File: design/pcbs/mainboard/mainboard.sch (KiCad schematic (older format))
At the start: 15 parts, among them J1 Conn_Coaxial, J15 Conn_01x01, J16 Conn_01x01, J17 Conn_01x01, J18 Conn_01x01, J2 Conn_Coaxial, J4 AudioJackSw

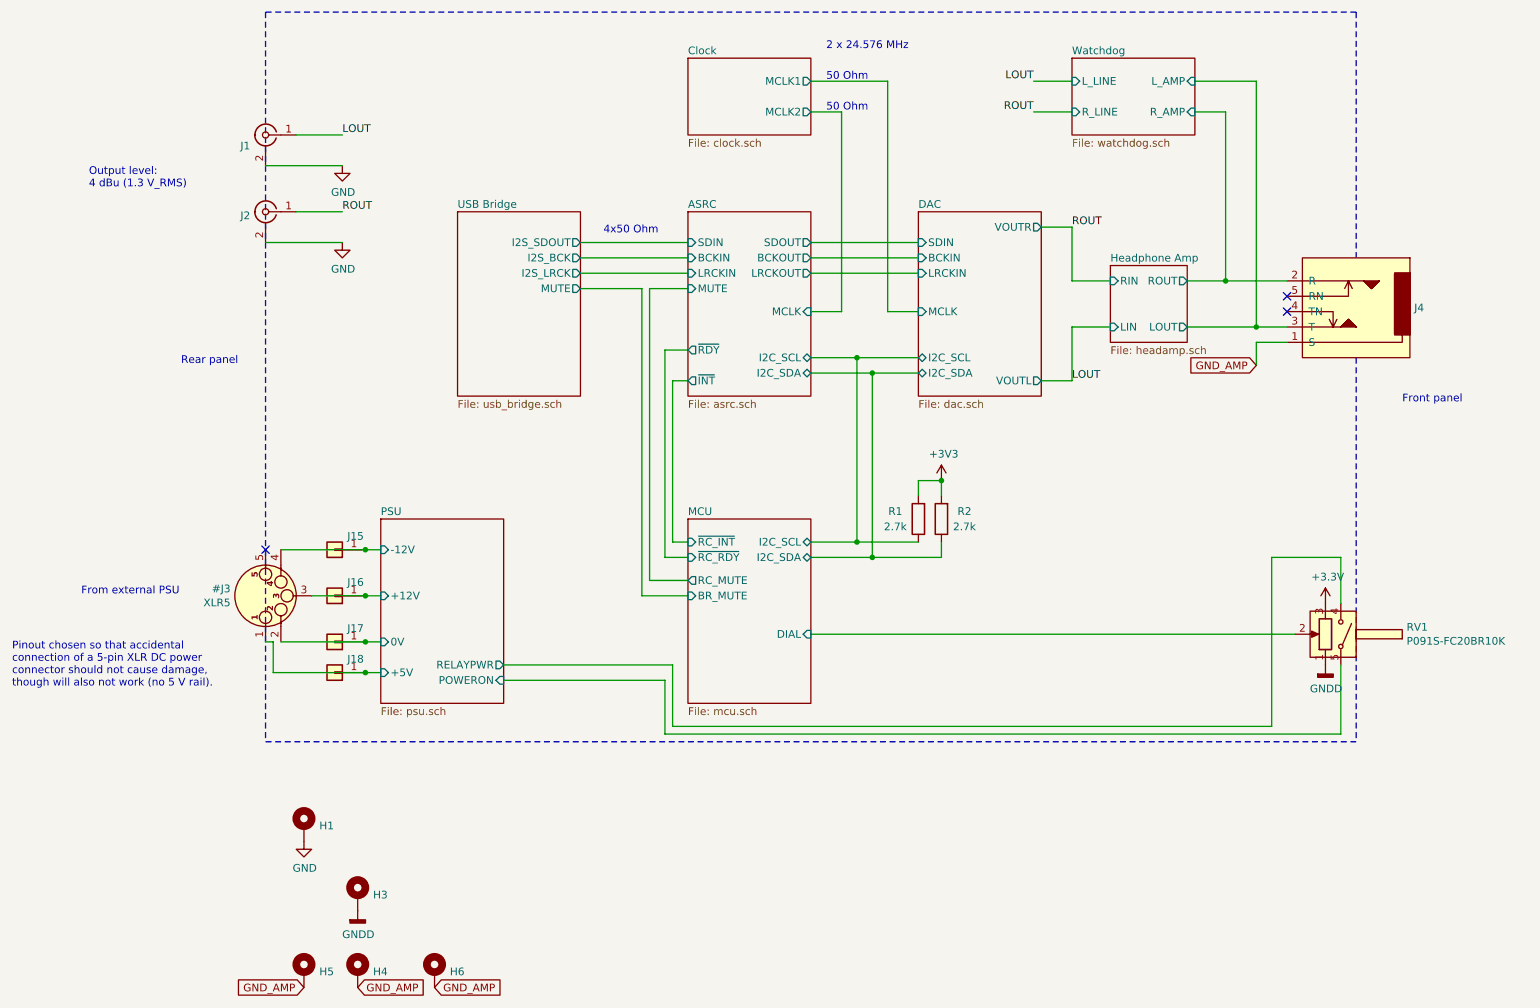
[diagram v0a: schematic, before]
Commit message: Renumbered footprints to follow board position.
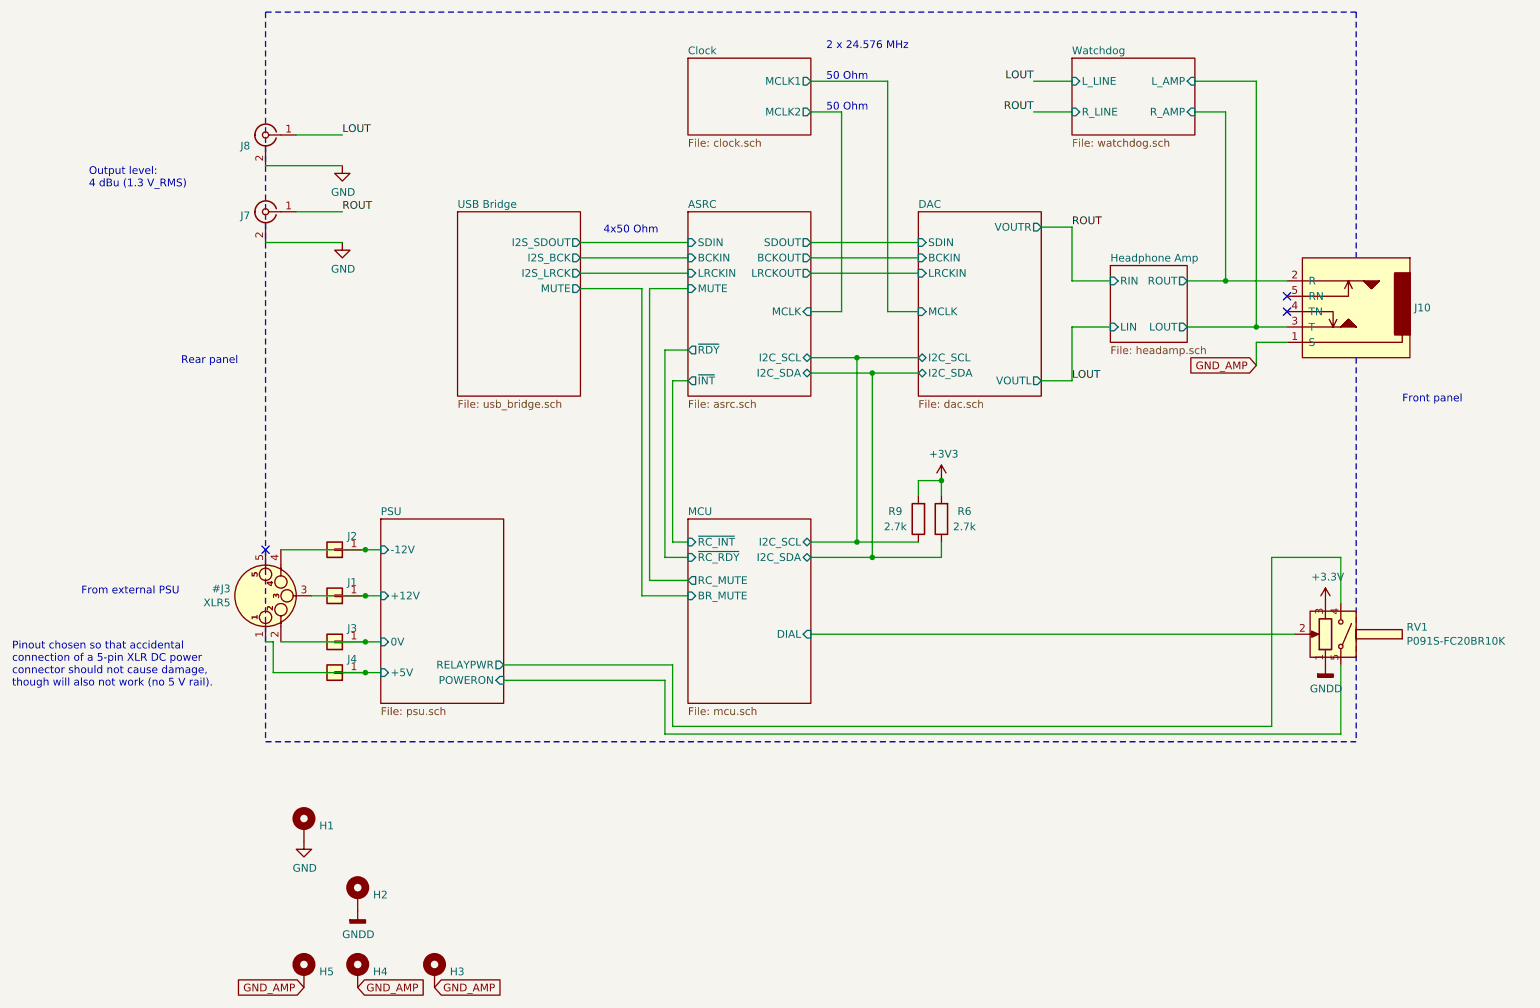
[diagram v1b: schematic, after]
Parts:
- renumbered H3 to H2, H6 to H3, J16 to J1, J4 to J10, J15 to J2, J17 to J3, J18 to J4, J2 to J7, J1 to J8, R2 to R6, R1 to R9
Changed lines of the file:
@@
 	4300 2900 5000 2900
 $Comp
-L Device:R R1
+L Device:R R9
 U 1 1 5ECF9309
 P 6500 4500
-F 0 "R1" H 6650 4450 50  0000 C CNN
+F 0 "R9" H 6650 4450 50  0000 C CNN
 F 1 "2.7k" H 6650 4550 50  0000 C CNN
 F 2 "Resistor_SMD:R_0402_1005Metric" V 6430 4500 50  0001 C CNN
@@
 $EndComp
 $Comp
-L Device:R R2
+L Device:R R6
 U 1 1 5ECF9BAA
 P 6650 4500
-F 0 "R2" H 6500 4450 50  0000 C CNN
+F 0 "R6" H 6500 4450 50  0000 C CNN
 F 1 "2.7k" H 6500 4550 50  0000 C CNN
 F 2 "Resistor_SMD:R_0402_1005Metric" V 6580 4500 50  0001 C CNN
@@
 $EndComp
 $Comp
-L Connector:Conn_Coaxial J2
+L Connector:Conn_Coaxial J7
 U 1 1 5ECDAB0B
 P 2250 2500
-F 0 "J2" H 2350 2475 50  0000 L CNN
+F 0 "J7" H 2350 2475 50  0000 L CNN
 F 1 "Conn_Coaxial" H 2350 2384 50  0001 L CNN
 F 2 "Connector_Wire:SolderWirePad_1x02_P5.08mm_Drill1.5mm" H 2250 2500 50  0001 C CNN
@@
 $EndComp
 $Comp
-L Connector:Conn_Coaxial J1
+L Connector:Conn_Coaxial J8
 U 1 1 5ECD9A3B
 P 2250 2000
-F 0 "J1" H 2350 1929 50  0000 L CNN
+F 0 "J8" H 2350 1929 50  0000 L CNN
 F 1 "Conn_Coaxial" H 2350 1884 50  0001 L CNN
 F 2 "Connector_Wire:SolderWirePad_1x02_P5.08mm_Drill1.5mm" H 2250 2000 50  0001 C CNN
@@
 Front panel
 $Comp
-L dac:AudioJackSw J4
+L dac:AudioJackSw J10
 U 1 1 5ED7F1B2
 P 9350 3150
-F 0 "J4" H 8972 3175 50  0000 R CNN
+F 0 "J10" H 8972 3175 50  0000 R CNN
 F 1 "AudioJackSw" H 8972 3130 50  0001 R CNN
 F 2 "mainboard:Amphenol_ACJS-MHOM" H 8650 2650 50  0001 C CNN
@@
 P 2700 4700
 AR Path="/5EC7824B/5EE2FF16" Ref="J?"  Part="1"
-AR Path="/5EE2FF16" Ref="J15"  Part="1"
-F 0 "J15" H 2618 4612 50  0000 R CNN
+AR Path="/5EE2FF16" Ref="J2"  Part="1"
+F 0 "J2" H 2618 4612 50  0000 R CNN
 F 1 "Conn_01x01" V 2573 4612 50  0001 R CNN
 F 2 "Connector_Wire:SolderWirePad_1x01_Drill1.5mm" H 2700 4700 50  0001 C CNN
@@
 P 2700 5000
 AR Path="/5EC7824B/5EE31BA3" Ref="J?"  Part="1"
-AR Path="/5EE31BA3" Ref="J16"  Part="1"
-F 0 "J16" H 2618 4912 50  0000 R CNN
+AR Path="/5EE31BA3" Ref="J1"  Part="1"
+F 0 "J1" H 2618 4912 50  0000 R CNN
 F 1 "Conn_01x01" V 2573 4912 50  0001 R CNN
 F 2 "Connector_Wire:SolderWirePad_1x01_Drill1.5mm" H 2700 5000 50  0001 C CNN
@@
 P 2700 5300
 AR Path="/5EC7824B/5EE33A2C" Ref="J?"  Part="1"
-AR Path="/5EE33A2C" Ref="J17"  Part="1"
-F 0 "J17" H 2618 5212 50  0000 R CNN
+AR Path="/5EE33A2C" Ref="J3"  Part="1"
+F 0 "J3" H 2618 5212 50  0000 R CNN
 F 1 "Conn_01x01" V 2573 5212 50  0001 R CNN
 F 2 "Connector_Wire:SolderWirePad_1x01_Drill1.5mm" H 2700 5300 50  0001 C CNN
@@
 P 2700 5500
 AR Path="/5EC7824B/5EE35FBE" Ref="J?"  Part="1"
-AR Path="/5EE35FBE" Ref="J18"  Part="1"
-F 0 "J18" H 2618 5412 50  0000 R CNN
+AR Path="/5EE35FBE" Ref="J4"  Part="1"
+F 0 "J4" H 2618 5412 50  0000 R CNN
 F 1 "Conn_01x01" V 2573 5412 50  0001 R CNN
 F 2 "Connector_Wire:SolderWirePad_1x01_Drill1.5mm" H 2700 5500 50  0001 C CNN
@@
 	8700 3350 8700 3500
 $Comp
-L Mechanical:MountingHole_Pad H3
+L Mechanical:MountingHole_Pad H2
 U 1 1 5EE3E32B
 P 2850 6950
-F 0 "H3" H 2950 6953 50  0000 L CNN
+F 0 "H2" H 2950 6953 50  0000 L CNN
 F 1 "MountingHole" H 2950 6908 50  0001 L CNN
 F 2 "MountingHole:MountingHole_3.2mm_M3_Pad_Via" H 2850 6950 50  0001 C CNN
@@
 $EndComp
 $Comp
-L Mechanical:MountingHole_Pad H6
+L Mechanical:MountingHole_Pad H3
 U 1 1 5EE96C34
 P 3350 7450
-F 0 "H6" H 3450 7453 50  0000 L CNN
+F 0 "H3" H 3450 7453 50  0000 L CNN
 F 1 "MountingHole" H 3450 7408 50  0001 L CNN
 F 2 "MountingHole:MountingHole_3.2mm_M3_Pad_Via" H 3350 7450 50  0001 C CNN

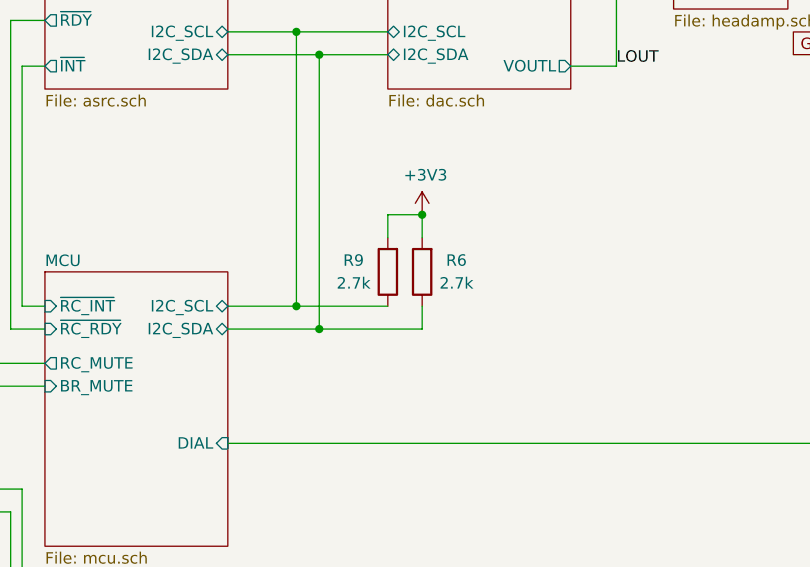
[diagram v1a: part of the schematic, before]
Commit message: Fixed title blocks. Added fab outputs.
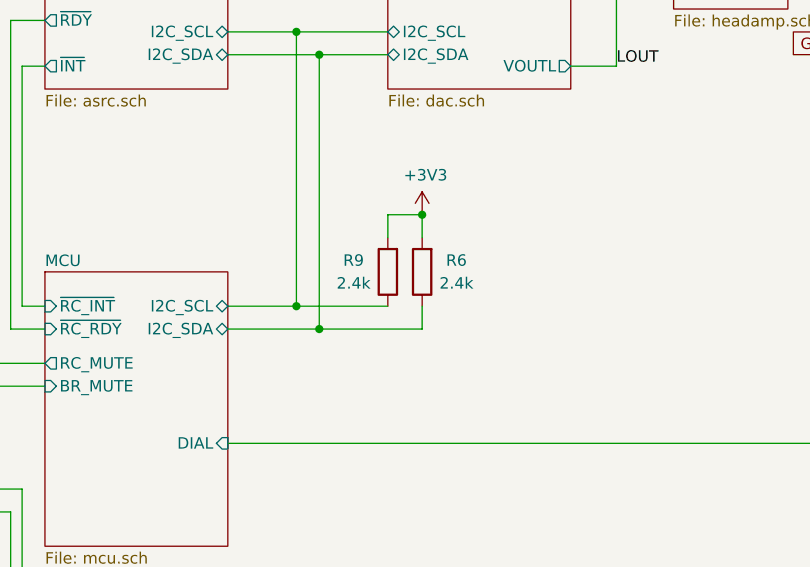
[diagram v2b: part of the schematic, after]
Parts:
- R6, R9: value 2.7k -> 2.4k; LCSC C25885 -> C25882
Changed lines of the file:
@@
 encoding utf-8
 Sheet 1 10
-Title ""
-Date ""
-Rev ""
-Comp ""
-Comment1 ""
-Comment2 ""
+Title "DAC1 Main board"
+Date "2020-06-27"
+Rev "1.0.0"
+Comp "© Mark Pinese 2020"
+Comment1 "To view a copy of this license, visit https://creativecommons.org/licenses/by/4.0"
+Comment2 "This work is licensed under CC BY 4.0."
 Comment3 ""
 Comment4 ""
@@
 P 6500 4500
 F 0 "R9" H 6650 4450 50  0000 C CNN
-F 1 "2.7k" H 6650 4550 50  0000 C CNN
+F 1 "2.4k" H 6650 4550 50  0000 C CNN
 F 2 "Resistor_SMD:R_0402_1005Metric" V 6430 4500 50  0001 C CNN
-F 3 "https://datasheet.lcsc.com/szlcsc/Uniroyal-Elec-0402WGF2701TCE_C25885.pdf" H 6500 4500 50  0001 C CNN
-F 4 "C25885" H 6500 4500 50  0001 C CNN "LCSC"
+F 3 "https://datasheet.lcsc.com/szlcsc/Uniroyal-Elec-0402WGF2401TCE_C25882.pdf" H 6500 4500 50  0001 C CNN
+F 4 "C25882" H 6500 4500 50  0001 C CNN "LCSC"
 F 5 "Yes" H 6500 4500 50  0001 C CNN "Done"
 F 6 "Pullup" H 6500 4500 50  0001 C CNN "Function"
@@
 P 6650 4500
 F 0 "R6" H 6500 4450 50  0000 C CNN
-F 1 "2.7k" H 6500 4550 50  0000 C CNN
+F 1 "2.4k" H 6500 4550 50  0000 C CNN
 F 2 "Resistor_SMD:R_0402_1005Metric" V 6580 4500 50  0001 C CNN
-F 3 "https://datasheet.lcsc.com/szlcsc/Uniroyal-Elec-0402WGF2701TCE_C25885.pdf" H 6650 4500 50  0001 C CNN
-F 4 "C25885" H 6650 4500 50  0001 C CNN "LCSC"
+F 3 "Uniroyal-Elec-0402WGF2401TCE_C25882.pdf" H 6650 4500 50  0001 C CNN
+F 4 "C25882" H 6650 4500 50  0001 C CNN "LCSC"
 F 5 "Yes" H 6650 4500 50  0001 C CNN "Done"
 F 6 "Pullup" H 6650 4500 50  0001 C CNN "Function"
